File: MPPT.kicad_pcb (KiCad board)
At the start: 2 copper layers, 125 x 145 mm, 136 parts, among them J1 Car Power, J2 Solar Array, J3 Battery, J4 CAN_In, J5 CAN_Out, Q1 NMOS, Q2 NMOS, SW1 RESET, SW2 SW_DIP_x02, U1 Nucleo_L432KC, U2 UCC37321, U3 PQMC3-D12-S9-S, U4 INA210, U5 INA210, U6 MAX40075AUT+, U7 MAX40075AUT+, U8 ADM3055E, U9 CDSOT23-T24CAN

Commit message: savestate
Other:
- net class Default removed
- net class HighPower removed
- net class HighPowerHalf removed
- net class HighPowerSignal removed
- net class HighPowerSmall removed
- net class LowPower removed
- net class Signal removed
- rule pad_to_mask_clearance: 0.2 -> 0

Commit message: schematic and layout revision.
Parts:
- removed C22: 10uF, Capacitor_SMD:C_0805_2012Metric
- removed C23: 0.01uF, Capacitor_SMD:C_0805_2012Metric
- removed C24: 0.1uF, Capacitor_SMD:C_0805_2012Metric
- removed D11, D13: 3.9V Zener, Diode_SMD:D_SOD-123F
- removed D12, D14: Diode, Diode_SMD:D_SOD-123F
- removed G***: LOGO, UTSVT_Special:Hallock_Image_Tiny
- removed G***: LOGO, UTSVT_Special:UTSVT_Logo_Symbol
- removed R23: 1.7k, Resistor_SMD:R_0805_2012Metric
- removed R24: 0, Resistor_SMD:R_0805_2012Metric
- removed R25, R26: 60, Resistor_SMD:R_0805_2012Metric
- added CP1: 1000uF, Capacitor_THT:CP_Radial_D30.0mm_P10.00mm_SnapIn, F.Cu at (125.6, 110.4)
- added CP2: 1000uF, Capacitor_THT:CP_Radial_D30.0mm_P10.00mm_SnapIn, F.Cu at (84.2, 110.1)
- added J6: CAN_Out, Connector_Molex:Molex_Micro-Fit_3.0_43650-0415_1x04_P3.00mm_Vertical, F.Cu at (40.8, 148.2)
- added TP29: CAN_ISO_GndOut, TestPoint:TestPoint_Pad_1.0x1.0mm, B.Cu at (39.8, 129.7)
- added TP30: CAN_H, TestPoint:TestPoint_Pad_1.0x1.0mm, B.Cu at (33.8, 129.7)
- added TP31: CAN_L, TestPoint:TestPoint_Pad_1.0x1.0mm, B.Cu at (31.8, 129.7)
- added U10: CDSOT23-T24CAN, Package_TO_SOT_SMD:SOT-23, F.Cu at (33.4, 141.6)
- C1: value 0.1uF -> 10uF; moved to B.Cu
- C10: value 1000uF -> 100nF; footprint Capacitor_THT:CP_Radial_D30.0mm_P10.00mm_SnapIn -> Capacitor_SMD:C_0805_2012Metric; moved to B.Cu
- C11, C13: value 0.1uF -> 100nF
- C12: value 1uF -> 100nF
- C14, C2: value 1uF -> 10uF
- C15, C16: value 1uF -> 100nF; moved to B.Cu
- C17: value 10uF -> 10nF
- C18: value 0.1uF -> 220nF
- C19: value 0.1uF -> 10uF
- C20: value 0.01uF -> 100nF
- C21: value 0.22uF -> 10nF
- C3: value 0.1uF -> 100nF; moved to B.Cu
- C4: value 100uF -> 100nF; footprint Capacitor_SMD:C_1210_3225Metric -> Capacitor_SMD:C_0805_2012Metric; moved to B.Cu
- C5: value 47uF -> 1uF; footprint Capacitor_SMD:C_1210_3225Metric -> Capacitor_SMD:C_0805_2012Metric; moved to B.Cu
- C6: value 10uF -> 4.7uF; moved to B.Cu
- C7: value 100uF -> 4.7uF; footprint Capacitor_SMD:C_1210_3225Metric -> Capacitor_SMD:C_0805_2012Metric; moved to B.Cu
- C8: value 1000uF -> 2.2uF; footprint Capacitor_THT:CP_Radial_D30.0mm_P10.00mm_SnapIn -> Capacitor_SMD:C_0805_2012Metric; moved to B.Cu
- C9: value CP -> CP?
- D1: value 3.9V Zener -> 13.2V; footprint Diode_SMD:D_SOD-123F -> Diode_SMD:D_SOD-323F
- D10, D2, D8: value Diode -> 3.3V Zener; footprint Diode_SMD:D_SOD-123F -> Diode_SMD:D_MiniMELF
- D3: moved to B.Cu
- D7, D9: value 3.9V Zener -> 3.3V Zener; footprint Diode_SMD:D_SOD-123F -> Diode_SMD:D_MiniMELF
- F1, F2: footprint MPPT-PrimaryPCB:05200101Z_Fuze_Holder_5x20_PCB_Mount -> MPPT:05200101Z_Fuze_Holder_5x20_PCB_Mount
- HS1: value Schottky Diode Heatsink -> MOSFET Heatsink
- HS3: value MOSFET Heatsink -> Schottky Diode Heatsink
- J2: value Solar Array -> 9V Supply; footprint MPPT-PrimaryPCB:PhoenixContact_PowerCombicon5_GF_2x7.62mm -> Connector_Molex:Molex_Micro-Fit_3.0_43650-0215_1x02_P3.00mm_Vertical
- J3: value Battery -> Solar Array; footprint MPPT-PrimaryPCB:PhoenixContact_PowerCombicon5_GF_2x7.62mm -> MPPT:PhoenixContact_PowerCombicon5_GF_2x7.62mm
- J4: value CAN_In -> Battery; footprint Connector_Molex:Molex_Micro-Fit_3.0_43650-0415_1x04_P3.00mm_Vertical -> MPPT:PhoenixContact_PowerCombicon5_GF_2x7.62mm
- J5: value CAN_Out -> CAN_In
- JP1: value Termination Resistors -> Jumper
- L1: value 4.7uH -> 6.8uH; footprint Inductor_SMD:L_0805_2012Metric -> Inductor_SMD:L_Taiyo-Yuden_NR-50xx; moved to B.Cu
- L2: footprint MPPT-PrimaryPCB:L_Toroid_Vertical_L46.0mm_W19.1mm_P21.80mm_Bourns_5700 -> MPPT:L_Toroid_Vertical_L46.0mm_W19.1mm_P21.80mm_Bourns_5700
- L3, L4: value 1.8kH -> 1.8kOhm; moved to F.Cu
- LED1: value Array Live (Green) -> 5V (Green)
- LED10: value BPS Full (Blue) -> Error (Amber)
- LED2: value Battery Live (Green) -> 9V (Green)
- LED3: value Car Power Live (Green) -> 9V (Green)
- LED4: value Device 9V Live (Green) -> 9V (Green)
- LED5: value Error (Amber) -> Heartbeat (Blue)
- LED8: value CAN_Tx (Blue) -> CAN_Rx (Blue)
- LED9: value CAN_Rx (Blue) -> CAN_Tx (Blue)
- R1: value 1.5 -> 330; moved to B.Cu
- R10, R8: value 330 -> 100k; moved to B.Cu
- R11: value 330 -> 2k; moved to B.Cu
- R12: value 10k -> 0
- R13: value R -> 60.4; footprint Package_TO_SOT_THT:TO-220-2_Vertical -> Resistor_SMD:R_0805_2012Metric; moved to B.Cu
- R14: value 2m -> 60.4; footprint Resistor_SMD:R_1206_3216Metric -> Resistor_SMD:R_0805_2012Metric
- R15: value 1.7k -> 15k
- R16: value 2m -> 27k; footprint Resistor_SMD:R_1206_3216Metric -> Resistor_SMD:R_0805_2012Metric
- R17: value 1.7k -> 330
- R18, R21: value 100k -> 330
- R19, R22: value 2k -> 330
- R2: value 15k -> 1.5; footprint Resistor_SMD:R_1206_3216Metric -> Resistor_SMD:R_0805_2012Metric
- R20: value 1.7k -> 330; moved to B.Cu
- R3: value 27k -> 330; footprint Resistor_SMD:R_1206_3216Metric -> Resistor_SMD:R_0805_2012Metric; moved to B.Cu
- R4: value 1.5k -> 10k; moved to B.Cu
- R5: value 1.1k -> R; footprint Resistor_SMD:R_0805_2012Metric -> Package_TO_SOT_THT:TO-220-2_Vertical
- R6, R7: value 330 -> 2m; footprint Resistor_SMD:R_0805_2012Metric -> Resistor_SMD:R_1206_3216Metric; moved to B.Cu
- R9: value 330 -> 3k; moved to B.Cu
- SW1: value RESET -> SW_Push
- SW2: footprint MPPT-PrimaryPCB:ADF02ST04_DIP_Switch_2_POS -> MPPT:ADF02ST04_DIP_Switch_2_POS
- TP1: value GND -> 12V; footprint TestPoint:TestPoint_Keystone_5005-5009_Compact -> TestPoint:TestPoint_Pad_1.0x1.0mm; moved to B.Cu
- TP10: value +SNUB -> GATE; footprint TestPoint:TestPoint_Keystone_5005-5009_Compact -> TestPoint:TestPoint_Pad_1.0x1.0mm; moved to B.Cu
- TP11: value +BATT -> +SNUB; footprint TestPoint:TestPoint_Keystone_5005-5009_Compact -> TestPoint:TestPoint_Pad_1.0x1.0mm; moved to B.Cu
- TP12: value -ARR -> M_SNUB; footprint TestPoint:TestPoint_Keystone_5005-5009_Compact -> TestPoint:TestPoint_Pad_1.0x1.0mm; moved to B.Cu
- TP13: value GATE -> -SNUB; footprint TestPoint:TestPoint_Keystone_5005-5009_Compact -> TestPoint:TestPoint_Pad_1.0x1.0mm; moved to B.Cu
- TP14: value M_SNUB -> GND; footprint TestPoint:TestPoint_Keystone_5005-5009_Compact -> TestPoint:TestPoint_Pad_1.0x1.0mm; moved to B.Cu
- TP15: value -SNUB -> -ARR; footprint TestPoint:TestPoint_Keystone_5005-5009_Compact -> TestPoint:TestPoint_Pad_1.0x1.0mm; moved to B.Cu
- TP16: value -BATT -> Array Current; footprint TestPoint:TestPoint_Keystone_5005-5009_Compact -> TestPoint:TestPoint_Pad_1.0x1.0mm; moved to B.Cu
- TP17: value Arr_I -> -BATT; footprint TestPoint:TestPoint_Keystone_5005-5009_Compact -> TestPoint:TestPoint_Pad_1.0x1.0mm; moved to B.Cu
- TP18: value Batt_I -> GND; footprint TestPoint:TestPoint_Keystone_5005-5009_Compact -> TestPoint:TestPoint_Pad_1.0x1.0mm; moved to B.Cu
- TP19: value Arr_V -> Battery Current; footprint TestPoint:TestPoint_Keystone_5005-5009_Compact -> TestPoint:TestPoint_Pad_1.0x1.0mm; moved to B.Cu
- TP2: value PWM -> Car GND; footprint TestPoint:TestPoint_Keystone_5005-5009_Compact -> TestPoint:TestPoint_Pad_1.0x1.0mm; moved to B.Cu
- TP20: value Batt_V -> +ARR; footprint TestPoint:TestPoint_Keystone_5005-5009_Compact -> TestPoint:TestPoint_Pad_1.0x1.0mm; moved to B.Cu
- TP21: value CAN_Tx -> Arr_V; footprint TestPoint:TestPoint_Keystone_5005-5009_Compact -> TestPoint:TestPoint_Pad_1.0x1.0mm; moved to B.Cu
- TP22: value CAN_Rx -> +BATT; footprint TestPoint:TestPoint_Keystone_5005-5009_Compact -> TestPoint:TestPoint_Pad_1.0x1.0mm; moved to B.Cu
- TP23: value CAN_ISO_Vout -> Batt_V; footprint TestPoint:TestPoint_Keystone_5005-5009_Compact -> TestPoint:TestPoint_Pad_1.0x1.0mm; moved to B.Cu
- TP24: value CAN_ISO_Vin -> CAN_Tx; footprint TestPoint:TestPoint_Keystone_5005-5009_Compact -> TestPoint:TestPoint_Pad_1.0x1.0mm; moved to B.Cu
- TP25: value CAN_ISO_GndIn -> CAN_Rx; footprint TestPoint:TestPoint_Keystone_5005-5009_Compact -> TestPoint:TestPoint_Pad_1.0x1.0mm; moved to B.Cu
- TP26: value CAN_ISO_GndOut -> CAN_ISO_Vout; footprint TestPoint:TestPoint_Keystone_5005-5009_Compact -> TestPoint:TestPoint_Pad_1.0x1.0mm; moved to B.Cu
- TP27: value CAN_H -> CAN_ISO_Vin; footprint TestPoint:TestPoint_Keystone_5005-5009_Compact -> TestPoint:TestPoint_Pad_1.0x1.0mm; moved to B.Cu
- TP28: value CAN_L -> CAN_ISO_GndIn; footprint TestPoint:TestPoint_Keystone_5005-5009_Compact -> TestPoint:TestPoint_Pad_1.0x1.0mm; moved to B.Cu
- TP3: value AGND -> +9V; footprint TestPoint:TestPoint_Keystone_5005-5009_Compact -> TestPoint:TestPoint_Pad_1.0x1.0mm; moved to B.Cu
- TP4: value PGND -> +3V3; footprint TestPoint:TestPoint_Keystone_5005-5009_Compact -> TestPoint:TestPoint_Pad_1.0x1.0mm; moved to B.Cu
- TP5: value Car +12V -> +5V; footprint TestPoint:TestPoint_Keystone_5005-5009_Compact -> TestPoint:TestPoint_Pad_1.0x1.0mm; moved to B.Cu
- TP6: value Car GND -> Board GND; footprint TestPoint:TestPoint_Keystone_5005-5009_Compact -> TestPoint:TestPoint_Pad_1.0x1.0mm; moved to B.Cu
- TP7: value +9VA -> PWM; footprint TestPoint:TestPoint_Keystone_5005-5009_Compact -> TestPoint:TestPoint_Pad_1.0x1.0mm; moved to B.Cu
- TP8: value Device GND -> AGND; footprint TestPoint:TestPoint_Keystone_5005-5009_Compact -> TestPoint:TestPoint_Pad_1.0x1.0mm; moved to B.Cu
- TP9: value +ARR -> 9VA; footprint TestPoint:TestPoint_Keystone_5005-5009_Compact -> TestPoint:TestPoint_Pad_1.0x1.0mm; moved to B.Cu
- U1: value Nucleo_L432KC -> RI3-1205S; footprint MPPT-PrimaryPCB:MODULE_NUCLEO-L432KC -> MPPT:CONV_RI3-1205S
- U2: value UCC37321 -> MCU_Nucleo_L432KC; footprint Package_SO:SOIC-8_3.9x4.9mm_P1.27mm -> MPPT:MODULE_NUCLEO-L432KC
- U3: value PQMC3-D12-S9-S -> UCC37321; footprint MPPT-PrimaryPCB:490_PQMC3_D12_S12_S -> Package_SO:SOIC-8_3.9x4.9mm_P1.27mm
- U4: value INA210 -> IES01_PDS1; footprint MPPT-PrimaryPCB:SC70-6 -> MPPT:IES01_PDS1; moved to F.Cu
- U5: footprint MPPT-PrimaryPCB:SC70-6 -> Package_DFN_QFN:UQFN-10_1.4x1.8mm_P0.4mm
- U6: value MAX40075AUT+ -> INA210; footprint Package_TO_SOT_SMD:SOT-23-6 -> Package_DFN_QFN:UQFN-10_1.4x1.8mm_P0.4mm; moved to B.Cu
- U7: value MAX40075AUT+ -> MAX40075; moved to B.Cu
- U8: value ADM3055E -> MAX40075; footprint MPPT-PrimaryPCB:ADM3055EBRIZ -> Package_TO_SOT_SMD:SOT-23-6; moved to B.Cu
- U9: value CDSOT23-T24CAN -> ADM3055E; footprint Package_TO_SOT_SMD:SOT-23 -> MPPT:ADM3055EBRIZ
- moved R5 120.7 mm to (99.8, 47.0), turned to 90 degrees
- moved J2 118.8 mm to (23.2, 64.7), turned to 90 degrees
- moved R13 117.5 mm to (34.7, 141.5), turned to -90 degrees
- moved J5 115.2 mm to (40.8, 157.0), turned to 180 degrees
- moved TP12 112.3 mm to (114.9, 41.3), turned to 180 degrees
- moved R2 107.9 mm to (53.6, 70.6)
- moved TP15 104.9 mm to (118.8, 133.5), turned to 180 degrees
- moved LED3 103.8 mm to (135.9, 146.5), turned to -90 degrees
- moved J4 103.7 mm to (75.0, 141.1)
- moved TP9 103.1 mm to (50.6, 71.3)
- moved R18 102.1 mm to (26.0, 98.4), turned to 180 degrees
- moved R19 98.3 mm to (26.0, 104.2)
- moved TP14 95.4 mm to (118.8, 130.6), turned to 180 degrees
- moved TP11 89.6 mm to (105.1, 47.3), turned to 180 degrees
- moved R4 86.9 mm to (59.9, 70.6), turned to -90 degrees
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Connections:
- C1 pad 1: GNDREF -> +12V
- C1 pad 2: +9VA -> GNDPWR
- C10 pad 1: /+Batt -> GND
- C10 pad 2: GNDREF -> +9VA
- C11 pad 1: +9VA -> GND
- C11 pad 2: GNDREF -> +9VA
- C12 pad 1: /Array_Current -> GND
- C12 pad 2: GNDREF -> +9VA
- C13 pad 1: +9VA -> GND
- C13 pad 2: GNDREF -> +9VA
- C14 pad 1: /Battery_Current -> +5V
- C14 pad 2: GNDREF -> GND
- C15 pad 1: Net-(C15-Pad1) -> GND
- C15 pad 2: GNDREF -> +5V
- C16 pad 1: Net-(C16-Pad1) -> GND
- C16 pad 2: GNDREF -> +3V3
- C17 pad 1: +5V -> +3V3
- C17 pad 2: GNDREF -> GND
- C18 pad 1: +5V -> Net-(C18-Pad1)
- C18 pad 2: GNDREF -> Net-(C18-Pad2)
- C19 pad 1: +3V3 -> Net-(C19-Pad1)
- C19 pad 2: GNDREF -> Net-(C19-Pad2)
- C2 pad 1: +9VA -> +5V
- C2 pad 2: GNDREF -> GND
- C20 pad 1: +3V3 -> Net-(C19-Pad2)
- C20 pad 2: GNDREF -> Net-(C19-Pad1)
- C21 pad 1: Net-(C21-Pad1) -> Net-(C19-Pad1)
- C21 pad 2: Net-(C21-Pad2) -> Net-(C19-Pad2)
- C3 pad 1: +9VA -> +9V
- C3 pad 2: GNDREF -> GND
- C4 pad 1: +12V -> GND
- C4 pad 2: GNDPWR -> +9VA
- C5 pad 1: Net-(C5-Pad1) -> +9VA
- C5 pad 2: GNDPWR -> GND
- C6 pad 1: GNDREF -> +5V
- C6 pad 2: Net-(C6-Pad2) -> GND
- C7 pad 1: +9VA -> Net-(C7-Pad1)
- C7 pad 2: GNDREF -> GND
- C8 pad 1: /+Arr -> +9VA
- C8 pad 2: GNDREF -> GND
- C9 pad 2: GNDREF -> GND
- D1 pad 1: /PWM -> +12V
- D1 pad 2: GNDREF -> GNDPWR
- D10 pad 1: /Battery_Current -> /Battery_Voltage
- D10 pad 2: GNDREF -> GND
- D2 pad 2: GNDREF -> GND
- D3 pad 2: GNDREF -> GND
- D5 pad 1: /+Batt -> /+BATT
- D6 pad 1: /+Batt -> /+BATT
- D7 pad 2: GNDREF -> GND
- D8 pad 1: /Array_Current -> /Battery_Current
- D8 pad 2: GNDREF -> GND
- D9 pad 1: /Battery_Current -> /Array_Voltage
- D9 pad 2: GNDREF -> GND
- F1 pad 1: Net-(F1-Pad1) -> /+ARR
- F1 pad 2: /+Arr -> Net-(F1-Pad2)
- F2 pad 2: /+Batt -> /+BATT
- J2 pad 1: Net-(F1-Pad1) -> +9V
- J2 pad 2: /-Arr -> GND
- J3 pad 1: Net-(F2-Pad1) -> Net-(F1-Pad2)
- J3 pad 2: /-Batt -> /-ARR
- J4 pad 1: Net-(C22-Pad1) -> Net-(F2-Pad1)
- J4 pad 2: Net-(C22-Pad2) -> /-BATT
- J5 pad 1: Net-(C22-Pad1) -> Net-(C19-Pad1)
- J5 pad 2: Net-(C22-Pad2) -> Net-(C19-Pad2)
- J5 pad 3: Net-(J4-Pad3) -> Net-(J5-Pad3)
- J5 pad 4: Net-(J4-Pad4) -> Net-(J5-Pad4)
- L1 pad 1: +12V -> +5V
- L1 pad 2: Net-(C5-Pad1) -> Net-(C7-Pad1)
- L2 pad 1: /+Arr -> /+ARR
- L3 pad 1: Net-(C22-Pad1) -> Net-(C19-Pad1)
- L3 pad 2: Net-(C21-Pad1) -> Net-(C18-Pad1)
- L4 pad 1: Net-(C22-Pad2) -> Net-(C19-Pad2)
- L4 pad 2: Net-(C21-Pad2) -> Net-(C18-Pad2)
- LED1 pad 1: /-Arr -> GND
- LED10 pad 1: GNDREF -> GND
- LED10 pad 2: Net-(LED10-Pad2) -> Net-(R22-Pad2)
- LED2 pad 1: /-Batt -> GND
- LED3 pad 1: GNDPWR -> /-ARR
- LED4 pad 1: GNDREF -> /-BATT
- LED5 pad 1: GNDREF -> GND
- LED6 pad 1: GNDREF -> GND
- LED7 pad 1: GNDREF -> GND
- LED8 pad 1: GNDREF -> GND
- LED9 pad 1: GNDREF -> GND
- Q1 pad 3: GNDREF -> GND
- Q2 pad 3: GNDREF -> GND
- R1 pad 1: /Drive_PWM -> +5V
- R1 pad 2: Net-(R1-Pad2) -> Net-(LED1-Pad2)
- R10 pad 1: Net-(LED9-Pad2) -> Net-(R10-Pad1)
- R10 pad 2: /CAN_Rx -> /+BATT
- R11 pad 1: Net-(LED10-Pad2) -> Net-(R10-Pad1)
- R11 pad 2: /BPS_Full -> GND
- R12 pad 1: /Drive_PWM -> Net-(R12-Pad1)
- R12 pad 2: GNDREF -> Net-(C19-Pad2)
- R13 pad 1: Net-(D4-Pad2) -> Net-(J5-Pad3)
- R13 pad 2: Net-(C9-Pad1) -> Net-(JP1-Pad1)
- R14 pad 1: GNDREF -> Net-(JP1-Pad2)
- R14 pad 2: /-Arr -> Net-(J5-Pad4)
- R15 pad 1: Net-(R15-Pad1) -> /+ARR
- R15 pad 2: /Array_Current -> Net-(LED3-Pad2)
- R16 pad 1: /-Batt -> /+BATT
- R16 pad 2: GNDREF -> Net-(LED4-Pad2)
- R17 pad 1: Net-(R17-Pad1) -> /Heartbeat
- R17 pad 2: /Battery_Current -> Net-(LED5-Pad2)
- R18 pad 1: /+Arr -> /Tracking
- R18 pad 2: Net-(R18-Pad2) -> Net-(LED6-Pad2)
- R19 pad 1: Net-(R18-Pad2) -> /PWM
- R19 pad 2: GNDREF -> Net-(LED7-Pad2)
- R2 pad 1: Net-(LED1-Pad2) -> Net-(R2-Pad1)
- R2 pad 2: /+Arr -> /Drive_PWM
- R20 pad 1: Net-(R18-Pad2) -> /CAN_Rx
- R20 pad 2: Net-(C15-Pad1) -> Net-(LED8-Pad2)
- R21 pad 1: /+Batt -> /CAN_Tx
- R21 pad 2: Net-(R21-Pad2) -> Net-(LED9-Pad2)
- R22 pad 1: Net-(R21-Pad2) -> /Error
- R22 pad 2: GNDREF -> Net-(R22-Pad2)
- R3 pad 1: Net-(LED2-Pad2) -> +9VA
- R3 pad 2: /+Batt -> Net-(LED2-Pad2)
- R4 pad 1: Net-(LED3-Pad2) -> /Drive_PWM
- R4 pad 2: +12V -> GND
- R5 pad 1: Net-(LED4-Pad2) -> Net-(D4-Pad2)
- R5 pad 2: +9VA -> Net-(C9-Pad1)
- R6 pad 1: Net-(LED5-Pad2) -> /-ARR
- R6 pad 2: /Error -> GND
- R7 pad 1: Net-(LED6-Pad2) -> GND
- R7 pad 2: /Tracking -> /-BATT
- R8 pad 1: Net-(LED7-Pad2) -> Net-(R8-Pad1)
- R8 pad 2: /PWM -> /+ARR
- R9 pad 1: Net-(LED8-Pad2) -> Net-(R8-Pad1)
- R9 pad 2: /CAN_Tx -> GND
- SW1 pad 1: /Reset -> GND
- SW1 pad 2: GNDREF -> /Reset
- SW2 pad 1: GNDREF -> GND
- SW2 pad 2: GNDREF -> GND
- TP1 pad 1: GNDREF -> +12V
- TP10 pad 1: Net-(D4-Pad2) -> /Drive_PWM
- TP11 pad 1: /+Batt -> Net-(D4-Pad2)
- TP12 pad 1: /-Arr -> Net-(C9-Pad1)
- TP13 pad 1: /Drive_PWM -> GND
- TP14 pad 1: Net-(C9-Pad1) -> GND
- TP15 pad 1: GNDREF -> /-ARR
- TP16 pad 1: /-Batt -> /Array_Current
- TP17 pad 1: /Array_Current -> /-BATT
- TP18 pad 1: /Battery_Current -> GND
- TP19 pad 1: /Array_Voltage -> /Battery_Current
- TP2 pad 1: /PWM -> GNDPWR
- TP20 pad 1: /Battery_Voltage -> /+ARR
- TP21 pad 1: /CAN_Tx -> /Array_Voltage
- TP22 pad 1: /CAN_Rx -> /+BATT
- TP23 pad 1: Net-(C21-Pad1) -> /Battery_Voltage
- TP24 pad 1: Net-(C22-Pad1) -> /CAN_Tx
- TP25 pad 1: Net-(C22-Pad2) -> /CAN_Rx
- TP26 pad 1: Net-(C21-Pad2) -> Net-(C18-Pad1)
- TP27 pad 1: Net-(J4-Pad3) -> Net-(C19-Pad1)
- TP28 pad 1: Net-(J4-Pad4) -> Net-(C19-Pad2)
- TP3 pad 1: GNDREF -> +9V
- TP4 pad 1: GNDREF -> +3V3
- TP5 pad 1: +12V -> +5V
- TP6 pad 1: GNDPWR -> GND
- TP7 pad 1: +9VA -> /PWM
- TP8 pad 1: GNDREF -> GND
- TP9 pad 1: /+Arr -> +9VA
- U1 pad 1: Net-(U1-Pad1) -> GNDPWR
- U1 pad 2: Net-(U1-Pad2) -> +12V
- U1 pad 3: /Reset -> GND
- U1 pad 4: GNDREF -> +5V
- U2 pad 1: +9VA -> /Heartbeat
- U2 pad 2: /PWM -> /Tracking
- U2 pad 3: /PWM -> /Reset
- U2 pad 4: GNDREF -> GND
- U2 pad 5: GNDREF -> /CAN_Tx
- U2 pad 6: Net-(R1-Pad2) -> /Error
- U2 pad 7: Net-(R1-Pad2) -> unconnected-(U2-Pad7)
- U2 pad 8: +9VA -> unconnected-(U2-Pad8)
- U3 pad 1: GNDPWR -> +9VA
- U3 pad 2: Net-(C5-Pad1) -> /PWM
- U3 pad 3: Net-(U3-Pad3) -> /PWM
- U3 pad 5: Net-(U3-Pad5) -> GND
- U3 pad 6: +9VA -> Net-(R2-Pad1)
- U3 pad 7: GNDREF -> Net-(R2-Pad1)
- U3 pad 8: Net-(C6-Pad2) -> +9VA
- U4 pad 1: GNDREF -> GND
- U4 pad 2: GNDREF -> Net-(C7-Pad1)
- U4 pad 4: GNDREF -> +9VA
- U4 pad 5: /-Arr -> GND
- U5 pad 1: GNDREF -> GND
- U5 pad 2: GNDREF -> GND
- U5 pad 4: /-Batt -> GND
- U5 pad 5: GNDREF -> /-ARR
- U5 pad 6: Net-(R17-Pad1) -> /Array_Current
- U6 pad 1: /Array_Voltage -> GND
- U6 pad 2: GNDREF -> GND
- U6 pad 3: Net-(C15-Pad1) -> +9VA
- U6 pad 4: /Array_Voltage -> /-BATT
- U6 pad 5: Net-(U6-Pad5) -> GND
- U6 pad 6: +3V3 -> /Battery_Current
- U7 pad 1: /Battery_Voltage -> /Array_Voltage
- U7 pad 2: GNDREF -> GND
- U7 pad 3: Net-(C16-Pad1) -> Net-(R8-Pad1)
- U7 pad 4: /Battery_Voltage -> /Array_Voltage
- U7 pad 5: Net-(U7-Pad5) -> GND
- U7 pad 6: +3V3 -> +9VA
- U8 pad 1: GNDREF -> /Battery_Voltage
- U8 pad 2: GNDREF -> GND
- U8 pad 3: +5V -> Net-(R10-Pad1)
- U8 pad 4: +3V3 -> /Battery_Voltage
- U8 pad 5: /CAN_Rx -> GND
- U8 pad 6: Net-(U8-Pad6) -> +9VA
- U9 pad 1: Net-(J4-Pad3) -> GND
- U9 pad 2: Net-(J4-Pad4) -> GND
- U9 pad 3: Net-(C22-Pad2) -> +5V
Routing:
- net GNDREF: track 149.6 -> 0.00 mm, vias 24 -> 0
- net /Array_Voltage: track 28.6 -> 151.3 mm, vias 1 -> 11
- net /Array_Current: track 24.2 -> 135.9 mm, vias 0 -> 7
- net Net-(D4-Pad2): track 153.9 -> 54.7 mm, vias 0 -> 1
- net +3V3: track 111.1 -> 17.7 mm, vias 5 -> 3
- net GND: track 0.00 -> 86.5 mm, vias 0 -> 20
- net /+ARR: track 0.00 -> 81.5 mm, vias 0 -> 2
- net Net-(R18-Pad2): track 71.2 -> 0.00 mm, vias 3 -> 0
- net /CAN_Rx: track 90.3 -> 19.4 mm, vias 5 -> 1
- net Net-(R15-Pad1): track 65.7 -> 0.00 mm, vias 2 -> 0
- net Net-(C22-Pad2): track 58.9 -> 0.00 mm, vias 1 -> 0
- net +9VA: track 204.9 -> 147.7 mm, vias 12 -> 10
- net Net-(C19-Pad2): track 0.00 -> 53.7 mm, vias 0 -> 6
- net Net-(C22-Pad1): track 47.5 -> 0.00 mm, vias 1 -> 0
- net /+BATT: track 0.00 -> 45.7 mm, vias 0 -> 2
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- added copper zone on F.Cu, net /+ARR
- added copper zone on F.Cu, net /+BATT
- added copper zone on B.Cu, net /-ARR
- added copper zone on B.Cu, net /-BATT
- added copper zone on B.Cu, net GND
- added copper zone on F.Cu, net Net-(D4-Pad2)
- added copper zone on F.Cu, net Net-(F1-Pad2)
- removed copper zone on F.Cu, net /+Arr
- removed copper zone on F.Cu, net /+Batt
- removed copper zone on B.Cu, net /-Arr
- removed copper zone on B.Cu, net /-Batt
- removed copper zone on B.Cu, net GNDREF
- removed copper zone on F.Cu, net Net-(F1-Pad1)
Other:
- board text added: "+3V3"
- board text added: "+5V"
- board text added: "+9V"
- board text added: "+ARR"
- board text added: "+BATT"
- board text added: "+SNUB"
- board text added: "-ARR"
- board text added: "-BATT"
- board text added: "-SNUB"
- board text added: "9V EXT"
- board text added: "ARRC"
- board text added: "ARRV"
- board text added: "BATTC"
- board text added: "BATTV"
- board text added: "CAN (it!)"
- board text added: "CANRX"
- board text added: "CANTX"
- board text added: "CAR 12V"
- board text added: "DRIVEPWM"
- board text added: "GND"
- board text added: "GNDOUT"
- board text added: "GNDPWR"
- board text added: "HEART"
- board text added: "LHR Solar Sunscatter MPPT v1.4.0 Spring 2022 Youssef Elsherif Gary Hallock Matthew Yu"
- board text added: "MSNUB"
- board text added: "NUCLEO-L432KC"
- board text added: "SETTINGS"
- board text removed: "+"
- board text removed: "-"
- board text removed: "AGND"
- board text removed: "ARR LIVE"
- board text removed: "ARR+"
- board text removed: "ARR_I"
- board text removed: "ARR_V"
- board text removed: "BATT LIVE"
- board text removed: "BATT+"
- board text removed: "BATT_I"
- board text removed: "BATT_V"
- board text removed: "BPS FULL"
- board text removed: "Board GND"
- board text removed: "CAN Circuit"
- board text removed: "CAN ID SELECT"
- board text removed: "CAN RX"
- board text removed: "CAN TX"
- board text removed: "CAN_RX"
- board text removed: "CAN_TX"
- board text removed: "Car GND"
- board text removed: "Car PWR"
- board text removed: "GND OUT"
- board text removed: "GNDREF"
- board text removed: "Gate"
- board text removed: "I could've just used B.Cu for CAN_TX and CAN_RX since GNDPWR isn't in the way, but I was unsure how much crosstalk the digital signal might get."
- board text removed: "In principle, I am concerned about routing thin analog signals across two power planes for high power systems. Especially in the case where the system is attempting to rapidly shift the voltage to maximize the current, sometimes in large steps, which may cause outsized current fluctuations and electromagnetic interference."
- board text removed: "PGND"
- board text removed: "Star ground separating digital logic from analog."
- board text removed: "U4"
- board text removed: "U5"
- board text removed: "UTSVT - Array MPPT v1.3 Fall 2020 Youssef Elsherif Gary Hallock Matthew Yu"
- board text removed: "Unused"

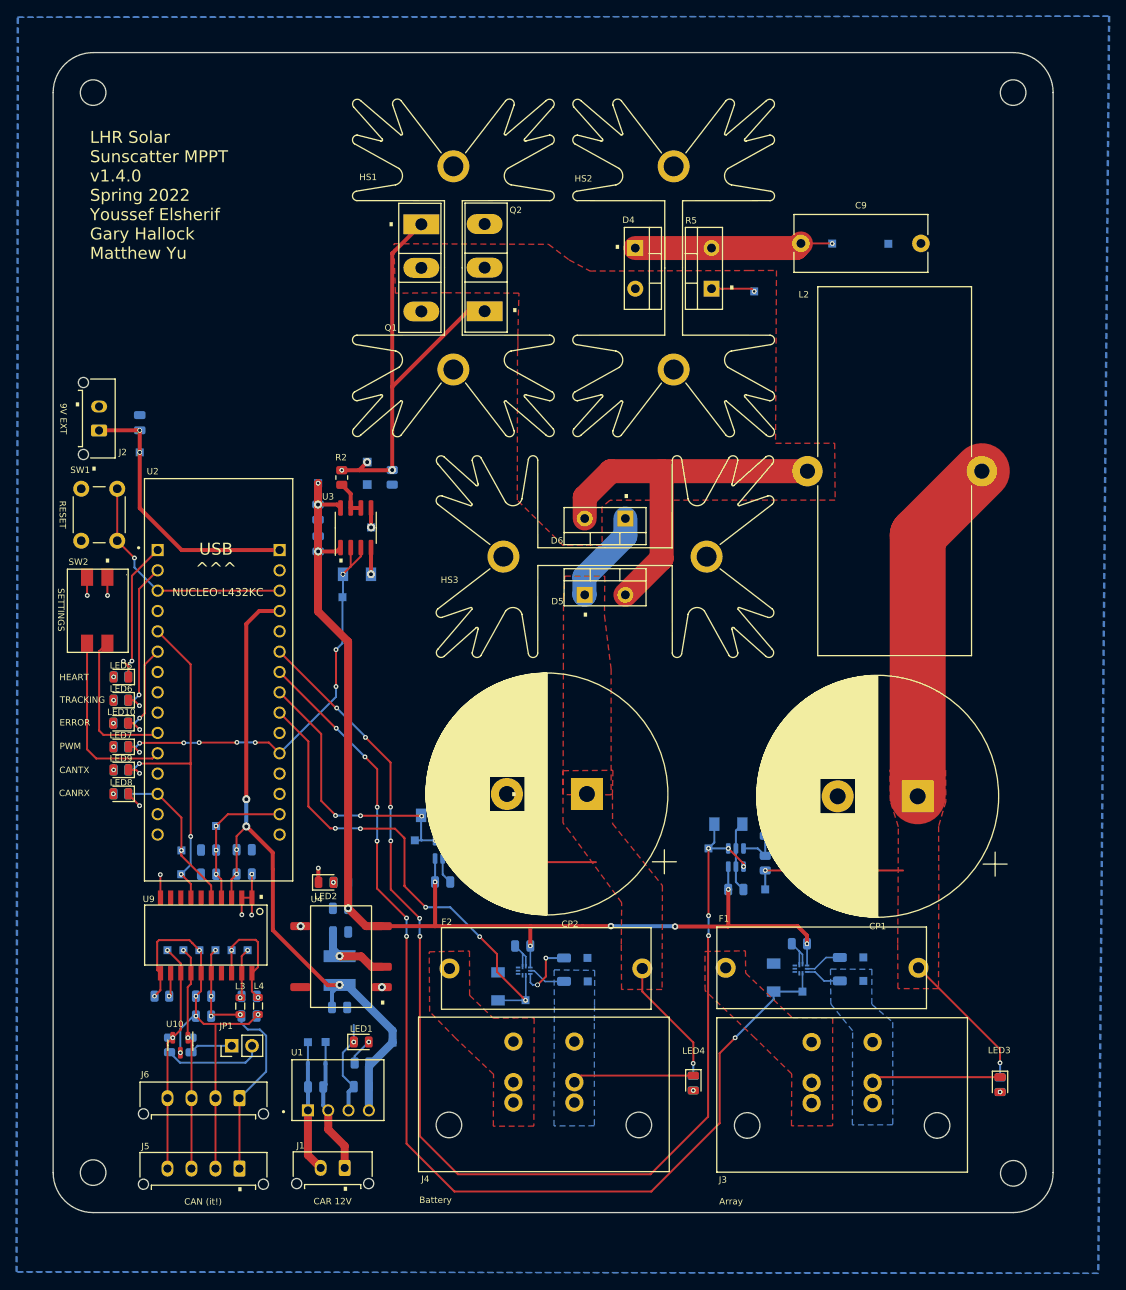
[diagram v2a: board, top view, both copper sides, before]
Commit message: secondary ground with via stitching
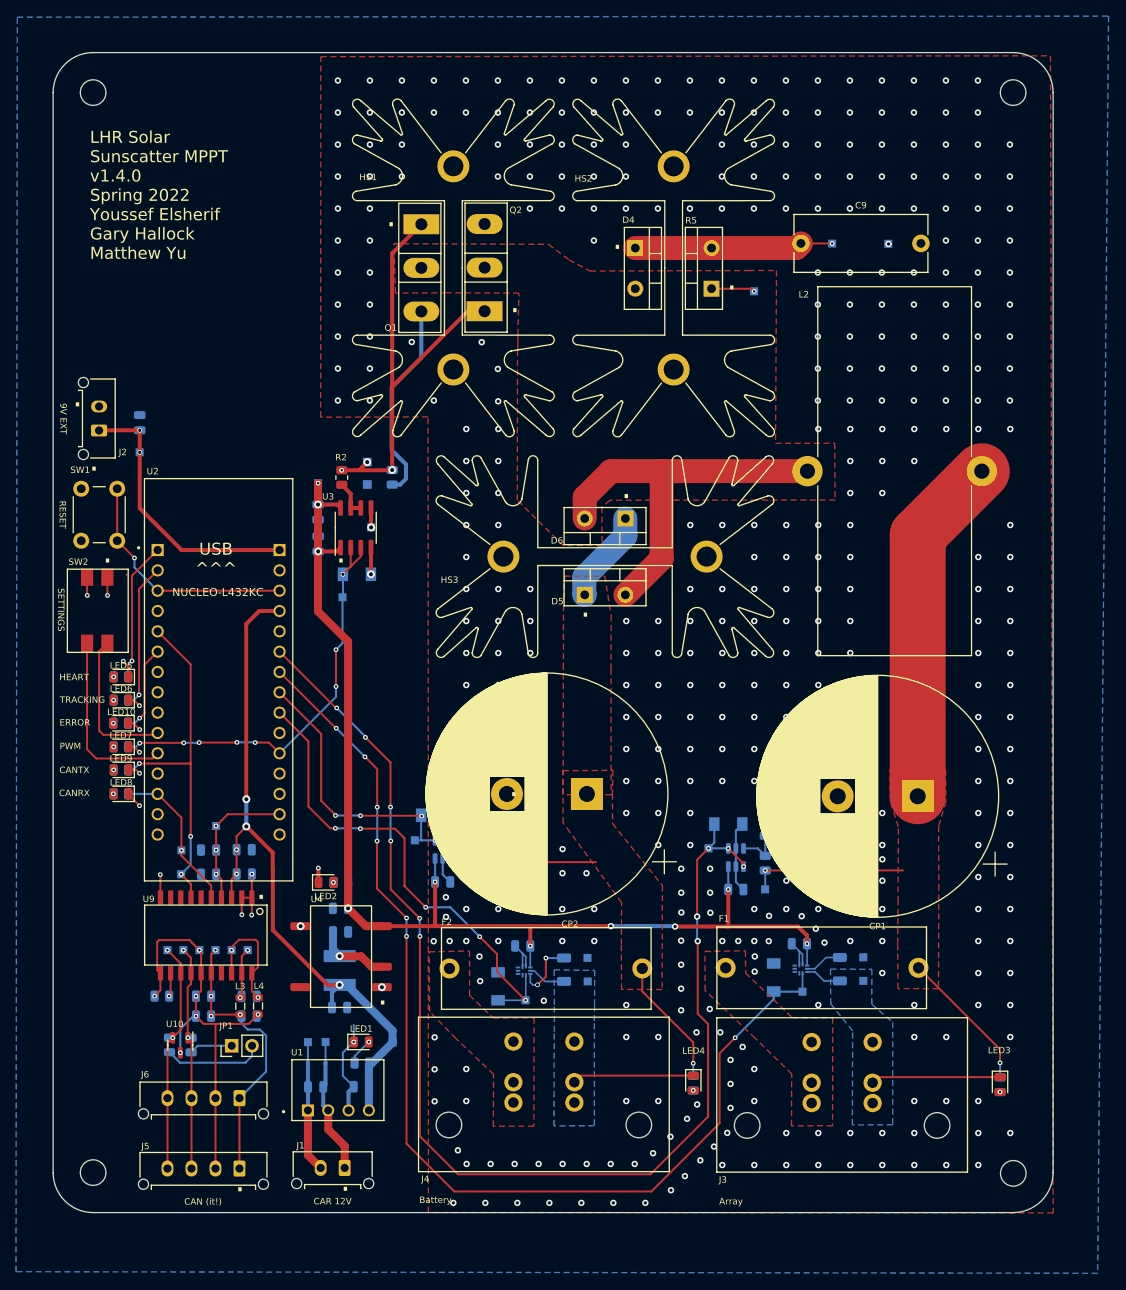
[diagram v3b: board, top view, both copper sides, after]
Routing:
- net GND: track 86.5 -> 111.7 mm, vias 20 -> 455
- net /Array_Voltage: track 151.3 -> 152.4 mm
- added copper zone on F.Cu, net GND

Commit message: Revisions on schematic and layout. See notes in the schematic for changes.
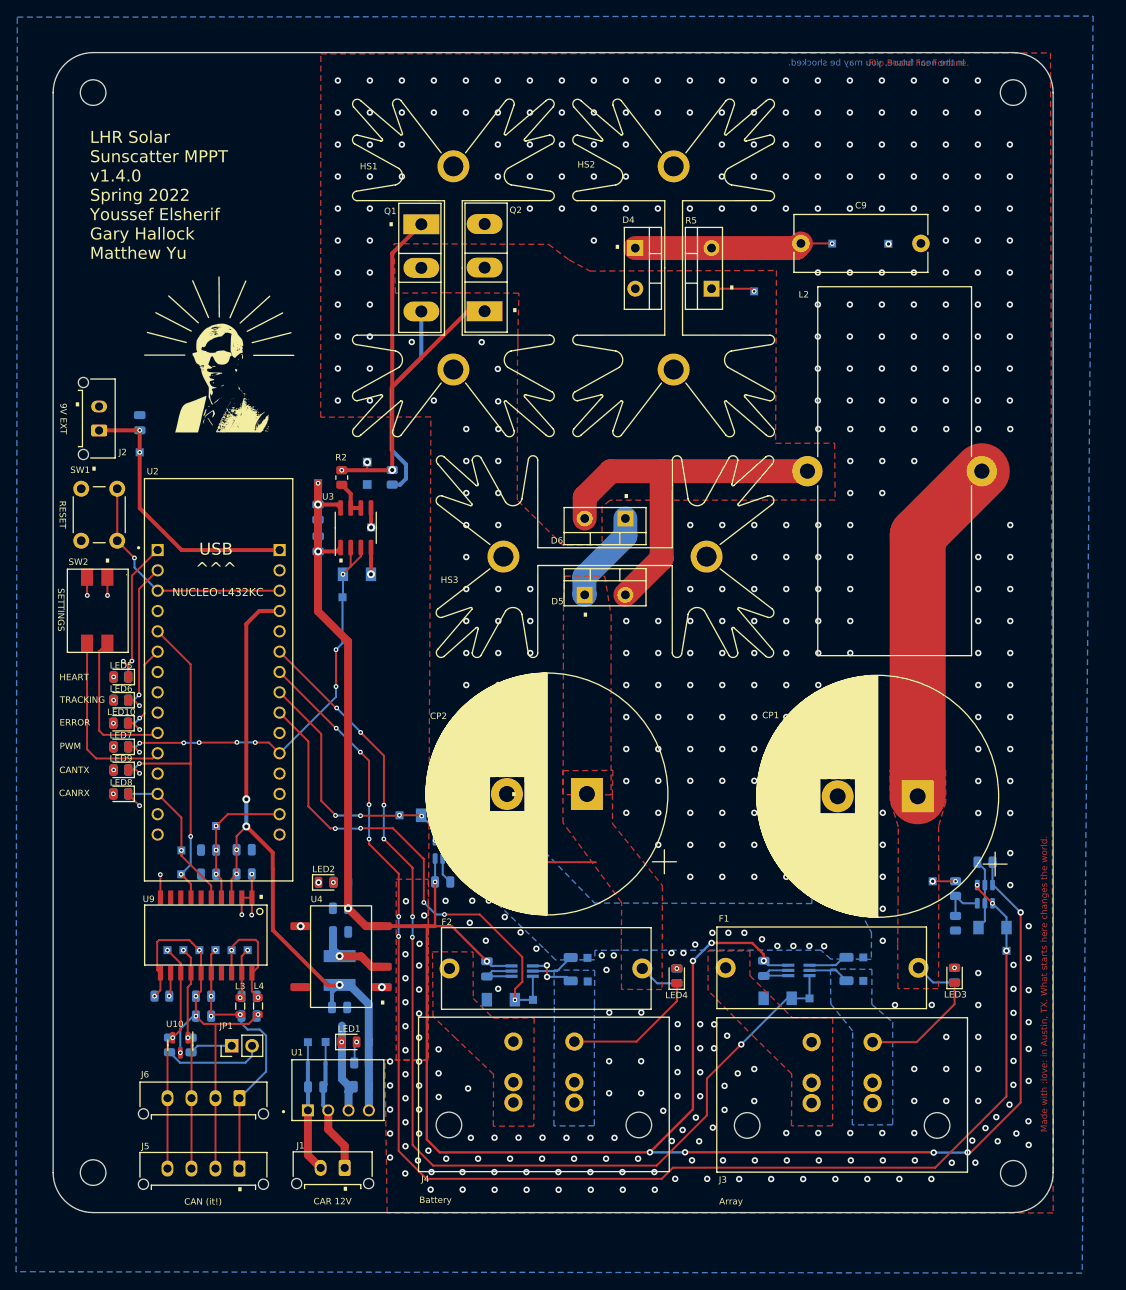
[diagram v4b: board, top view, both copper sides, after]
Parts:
- added G***: LOGO, UTSVT_Special:Hallock_Image_Tiny, F.Cu at (38.1, 58.0)
- added G***: LOGO, LOGO, B.Cu at (87.0, 66.2)
- added G***: LOGO, LOGO, B.Cu at (125.3, 89.5)
- added REF**: ESD-Logo_8.9x8mm_SilkScreen, Symbol:ESD-Logo_8.9x8mm_SilkScreen, B.Cu at (38.0, 91.0)
- added REF**: KiCad-Logo2_5mm_SilkScreen, Symbol:KiCad-Logo2_5mm_SilkScreen, B.Cu at (38.1, 99.2)
- U5, U6: footprint Package_DFN_QFN:UQFN-10_1.4x1.8mm_P0.4mm -> Package_TO_SOT_SMD:SOT-363_SC-70-6_Handsoldering
- moved TP21 39.4 mm to (136.7, 129.7), turned to 0 degrees
- moved D9 35.5 mm to (134.9, 126.8), turned to 180 degrees
- moved U7 31.5 mm to (134.0, 122.7), turned to 90 degrees
- moved C12 31.3 mm to (134.0, 118.7), turned to 0 degrees
- moved R9 26.6 mm to (130.3, 126.3), turned to -90 degrees
- moved R8 24.0 mm to (130.3, 122.0), turned to 90 degrees
- moved TP20 21.0 mm to (127.4, 121.1), turned to 0 degrees
- moved R15 14.8 mm to (130.2, 132.8), turned to 90 degrees
- moved LED3 14.8 mm to (130.2, 132.8), turned to 90 degrees
- moved R16 13.6 mm to (95.5, 132.9), turned to 90 degrees
- moved LED4 13.6 mm to (95.5, 132.9), turned to 90 degrees
- moved C10 5.41 mm to (106.3, 131.9), turned to 90 degrees
- moved C11 5.32 mm to (71.7, 132.0), turned to 90 degrees
- moved TP23 3.68 mm to (60.8, 112.8)
- moved TP5 2.95 mm to (57.0, 141.1)
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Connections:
- U2 pad 24: /Array_Current -> /Array_Voltage
- U2 pad 25: /Array_Voltage -> /Array_Current
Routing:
- net +9VA: track 147.7 -> 272.2 mm, vias 10 -> 14
- net /+ARR: track 81.5 -> 52.1 mm
- net /Array_Voltage: track 152.4 -> 175.8 mm, vias 11 -> 9
- net /+BATT: track 45.7 -> 34.7 mm, vias 2 -> 1
- net +5V: track 93.7 -> 84.8 mm
- net /-BATT: track 20.0 -> 23.5 mm, vias 0 -> 2
- net /Array_Current: track 135.9 -> 133.5 mm
- net /Battery_Voltage: track 37.9 -> 36.0 mm, vias 5 -> 6
- net GND: track 111.7 -> 110.5 mm, vias 455 -> 492
- net Net-(LED1-Pad2): track 3.36 -> 2.73 mm
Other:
- board text added: "2022 The year of the Kirbo car"
- board text added: "Contact: matthewjkyu@gmail.com"
- board text added: "Flip Board For Fortune."
- board text added: "Hey, we've trying to reach you concerning your vehicle's extended warranty..."
- board text added: "In the near future, you may be shocked."
- board text added: "Made with :love: in Austin, TX. What starts here changes the world."
- board text added: "This extra GND plane is covered by the larger GND plane. It serves to indicate the path where the return current from BATT- to ARR- is predicted to go."
